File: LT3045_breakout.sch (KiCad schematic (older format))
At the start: 11 parts, among them J1 CONN_01X03, U1 LT3045EDD

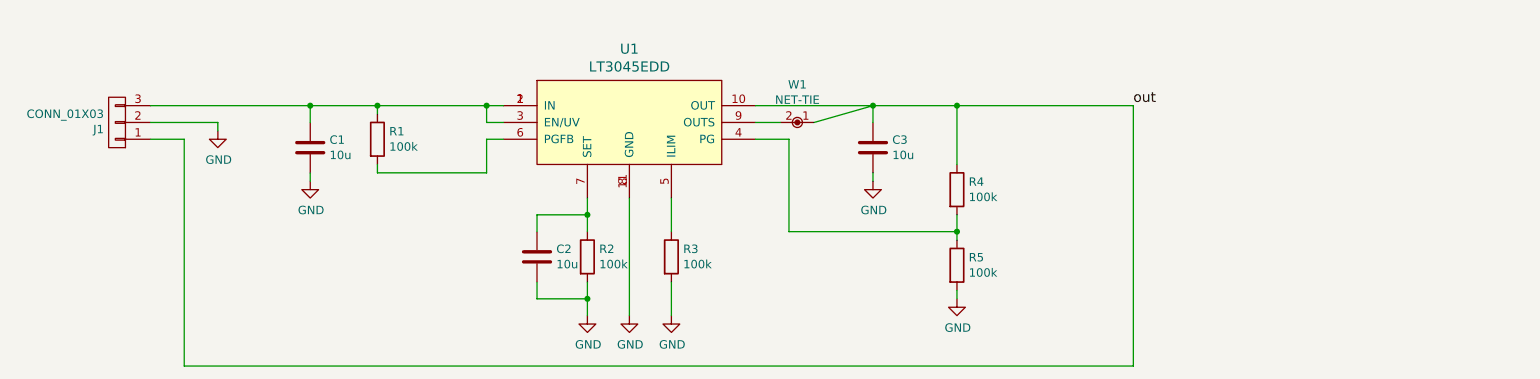
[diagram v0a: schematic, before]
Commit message: Removed PGFB pull resistor. We do not need that.
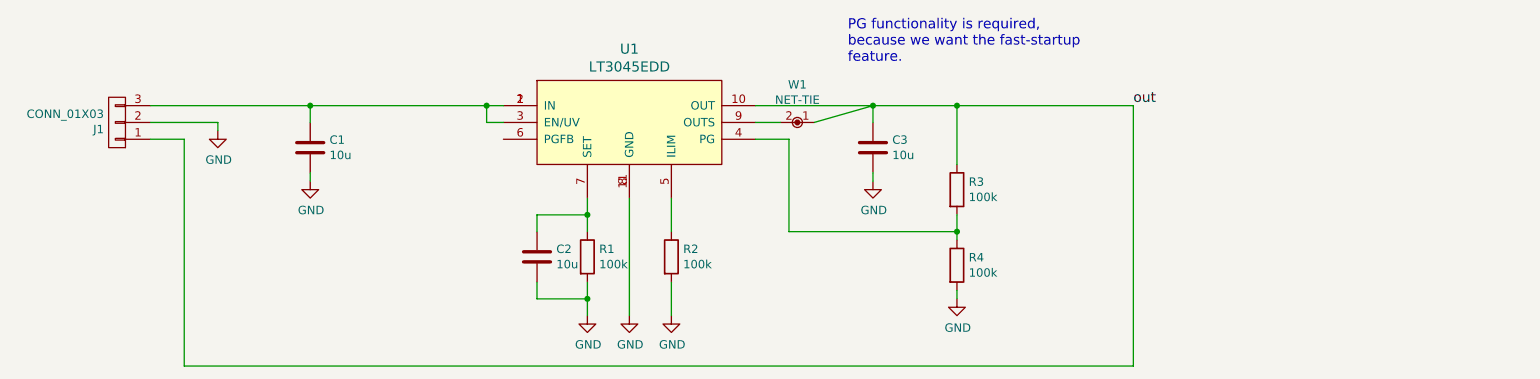
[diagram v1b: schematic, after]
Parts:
- removed R1: 100k, Resistors_SMD:R_0402, symbol R
- renumbered R2 to R1, R3 to R2, R4 to R3, R5 to R4
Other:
- note added: "PG functionality is required,\nbecause we want the fast-startup\nfeature."
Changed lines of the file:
@@
 LIBS:Linear Technology
 LIBS:net-tie
-LIBS:LT3045_breakout-cache
 EELAYER 26 0
 EELAYER END
@@
 $EndComp
 $Comp
-L GND #PWR01
+L GND #PWR1
 U 1 1 5989455D
 P 2600 2850
-F 0 "#PWR01" H 2600 2600 50  0001 C CNN
+F 0 "#PWR1" H 2600 2600 50  0001 C CNN
 F 1 "GND" H 2605 2677 50  0000 C CNN
 F 2 "" H 2600 2850 50  0001 C CNN
@@
 $EndComp
 Wire Wire Line
-	2200 2700 4300 2700
-$Comp
-L R R1
-U 1 1 59894789
-P 3550 2900
-F 0 "R1" H 3620 2946 50  0000 L CNN
-F 1 "100k" H 3620 2855 50  0000 L CNN
-F 2 "Resistors_SMD:R_0402" V 3480 2900 50  0001 C CNN
-F 3 "" H 3550 2900 50  0001 C CNN
-	1    3550 2900
-	1    0    0    -1
-$EndComp
-Wire Wire Line
-	3550 2700 3550 2750
-Connection ~ 3550 2700
-Wire Wire Line
-	3550 3050 3550 3100
-Wire Wire Line
-	3550 3100 4200 3100
-Wire Wire Line
-	4200 3100 4200 2900
-Wire Wire Line
-	4200 2900 4300 2900
-Wire Wire Line
 	4300 2800 4200 2800
 Wire Wire Line
@@
 Connection ~ 4200 2700
 $Comp
-L R R2
+L R R1
 U 1 1 5989486E
 P 4800 3600
-F 0 "R2" H 4870 3646 50  0000 L CNN
+F 0 "R1" H 4870 3646 50  0000 L CNN
 F 1 "100k" H 4870 3555 50  0000 L CNN
 F 2 "Resistors_SMD:R_0603" V 4730 3600 50  0001 C CNN
@@
 	4800 3750 4800 3950
 $Comp
-L GND #PWR02
+L GND #PWR3
 U 1 1 59894988
 P 4800 3950
-F 0 "#PWR02" H 4800 3700 50  0001 C CNN
+F 0 "#PWR3" H 4800 3700 50  0001 C CNN
 F 1 "GND" H 4805 3777 50  0000 C CNN
 F 2 "" H 4800 3950 50  0001 C CNN
@@
 	5050 3250 5050 3950
 $Comp
-L GND #PWR03
+L GND #PWR4
 U 1 1 598949D4
 P 5050 3950
-F 0 "#PWR03" H 5050 3700 50  0001 C CNN
+F 0 "#PWR4" H 5050 3700 50  0001 C CNN
 F 1 "GND" H 5055 3777 50  0000 C CNN
 F 2 "" H 5050 3950 50  0001 C CNN
@@
 $EndComp
 $Comp
-L R R3
+L R R2
 U 1 1 598949E9
 P 5300 3600
-F 0 "R3" H 5370 3646 50  0000 L CNN
+F 0 "R2" H 5370 3646 50  0000 L CNN
 F 1 "100k" H 5370 3555 50  0000 L CNN
 F 2 "Resistors_SMD:R_0603" V 5230 3600 50  0001 C CNN
@@
 $EndComp
 $Comp
-L GND #PWR04
+L GND #PWR5
 U 1 1 59894A27
 P 5300 3950
-F 0 "#PWR04" H 5300 3700 50  0001 C CNN
+F 0 "#PWR5" H 5300 3700 50  0001 C CNN
 F 1 "GND" H 5305 3777 50  0000 C CNN
 F 2 "" H 5300 3950 50  0001 C CNN
@@
 	6500 2700 6150 2800
 $Comp
-L R R4
-U 1 1 59894C9F
-P 7000 3200
-F 0 "R4" H 7070 3246 50  0000 L CNN
-F 1 "100k" H 7070 3155 50  0000 L CNN
-F 2 "Resistors_SMD:R_0402" V 6930 3200 50  0001 C CNN
-F 3 "" H 7000 3200 50  0001 C CNN
-	1    7000 3200
-	1    0    0    -1
-$EndComp
-$Comp
-L R R5
-U 1 1 59894D03
-P 7000 3650
-F 0 "R5" H 7070 3696 50  0000 L CNN
-F 1 "100k" H 7070 3605 50  0000 L CNN
-F 2 "Resistors_SMD:R_0402" V 6930 3650 50  0001 C CNN
-F 3 "" H 7000 3650 50  0001 C CNN
-	1    7000 3650
-	1    0    0    -1
-$EndComp
-Wire Wire Line
-	5800 2900 6000 2900
-Wire Wire Line
-	6000 2900 6000 3450
-Wire Wire Line
-	6000 3450 7000 3450
-Wire Wire Line
-	7000 3350 7000 3500
-Connection ~ 7000 3450
-$Comp
-L GND #PWR05
+L GND #PWR6
 U 1 1 59894DDD
 P 6500 3150
-F 0 "#PWR05" H 6500 2900 50  0001 C CNN
+F 0 "#PWR6" H 6500 2900 50  0001 C CNN
 F 1 "GND" H 6505 2977 50  0000 C CNN
 F 2 "" H 6500 3150 50  0001 C CNN
@@
 	1    0    0    -1
 $EndComp
-$Comp
-L GND #PWR06
-U 1 1 59894DFC
-P 7000 3850
-F 0 "#PWR06" H 7000 3600 50  0001 C CNN
-F 1 "GND" H 7005 3677 50  0000 C CNN
-F 2 "" H 7000 3850 50  0001 C CNN
-F 3 "" H 7000 3850 50  0001 C CNN
-	1    7000 3850
-	1    0    0    -1
-$EndComp
-Wire Wire Line
-	7000 3850 7000 3800
-Wire Wire Line
-	7000 2700 7000 3050
 Connection ~ 6500 2700
 Wire Wire Line
@@
 $EndComp
 $Comp
-L GND #PWR07
+L GND #PWR2
 U 1 1 59894F82
 P 3150 3150
-F 0 "#PWR07" H 3150 2900 50  0001 C CNN
+F 0 "#PWR2" H 3150 2900 50  0001 C CNN
 F 1 "GND" H 3155 2977 50  0000 C CNN
 F 2 "" H 3150 3150 50  0001 C CNN
@@
 Text Label 8050 2700 0    60   ~ 0
 out
+Wire Wire Line
+	7000 3850 7000 3800
+$Comp
+L GND #PWR7
+U 1 1 59894DFC
+P 7000 3850
+F 0 "#PWR7" H 7000 3600 50  0001 C CNN
+F 1 "GND" H 7005 3677 50  0000 C CNN
+F 2 "" H 7000 3850 50  0001 C CNN
+F 3 "" H 7000 3850 50  0001 C CNN
+	1    7000 3850
+	1    0    0    -1
+$EndComp
+Wire Wire Line
+	5800 2900 6000 2900
+Connection ~ 7000 3450
+Wire Wire Line
+	6000 2900 6000 3450
+Wire Wire Line
+	6000 3450 7000 3450
+Wire Wire Line
+	7000 3350 7000 3500
+$Comp
+L R R4
+U 1 1 59894D03
+P 7000 3650
+F 0 "R4" H 7070 3696 50  0000 L CNN
+F 1 "100k" H 7070 3605 50  0000 L CNN
+F 2 "Resistors_SMD:R_0402" V 6930 3650 50  0001 C CNN
+F 3 "" H 7000 3650 50  0001 C CNN
+	1    7000 3650
+	1    0    0    -1
+$EndComp
+Wire Wire Line
+	7000 2700 7000 3050
+$Comp
+L R R3
+U 1 1 59894C9F
+P 7000 3200
+F 0 "R3" H 7070 3246 50  0000 L CNN
+F 1 "100k" H 7070 3155 50  0000 L CNN
+F 2 "Resistors_SMD:R_0402" V 6930 3200 50  0001 C CNN
+F 3 "" H 7000 3200 50  0001 C CNN
+	1    7000 3200
+	1    0    0    -1
+$EndComp
+Text Notes 6350 2450 0    60   ~ 0
+PG functionality is required,\nbecause we want the fast-startup\nfeature.
+Wire Wire Line
+	2200 2700 4300 2700
 $EndSCHEMATC

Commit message: Changed resistor values to outout 12V@500mA
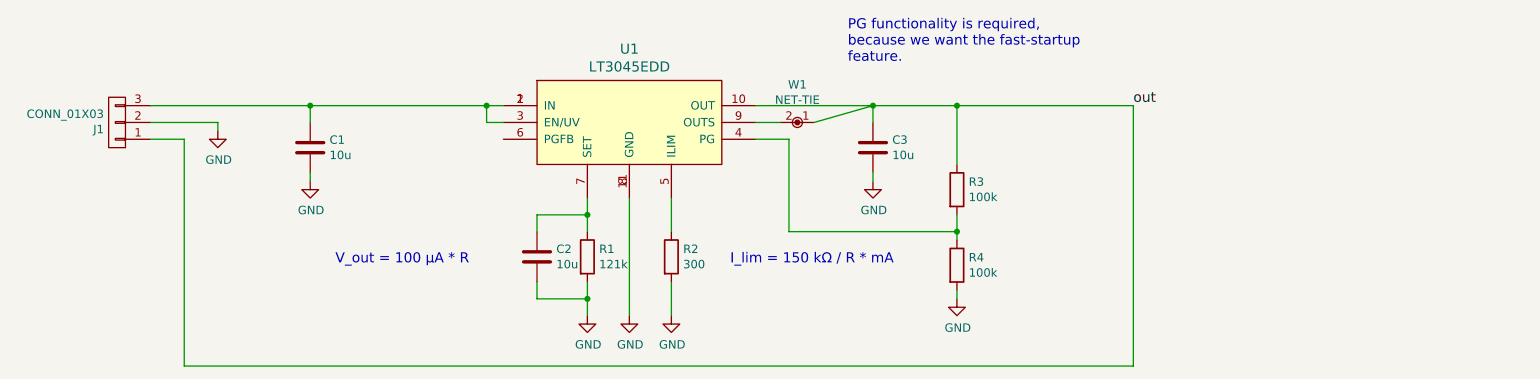
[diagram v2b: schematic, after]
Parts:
- R1: value 100k -> 121k
- R2: value 100k -> 300
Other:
- note added: "I_lim = 150 kΩ / R * mA"
- note added: "V_out = 100 µA * R"
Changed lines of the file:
@@
 LIBS:Linear Technology
 LIBS:net-tie
+LIBS:LT3045_breakout-cache
 EELAYER 26 0
 EELAYER END
@@
 P 4800 3600
 F 0 "R1" H 4870 3646 50  0000 L CNN
-F 1 "100k" H 4870 3555 50  0000 L CNN
+F 1 "121k" H 4870 3555 50  0000 L CNN
 F 2 "Resistors_SMD:R_0603" V 4730 3600 50  0001 C CNN
 F 3 "" H 4800 3600 50  0001 C CNN
@@
 P 5300 3600
 F 0 "R2" H 5370 3646 50  0000 L CNN
-F 1 "100k" H 5370 3555 50  0000 L CNN
+F 1 "300" H 5370 3555 50  0000 L CNN
 F 2 "Resistors_SMD:R_0603" V 5230 3600 50  0001 C CNN
 F 3 "" H 5300 3600 50  0001 C CNN
@@
 Wire Wire Line
 	2200 2700 4300 2700
+Text Notes 3300 3650 0    60   ~ 0
+V_out = 100 µA * R
+Text Notes 5650 3650 0    60   ~ 0
+I_lim = 150 kΩ / R * mA
 $EndSCHEMATC

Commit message: Updated to v1.1 Added BOM Removed old gerber files Updated component values on the pcb board
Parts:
- J1: symbol CONN_01X03 -> Conn_01x03_Male; MFN (none) -> Amphenol; MFP (none) -> 68016-403HLF
- R1: value 121k -> 120k; MFN (none) -> Susumu; MFP (none) -> RR0816P-124-D
- R2: MFN (none) -> Susumu; MFP (none) -> RR0816P-301-D
- R3: value 100k -> 200k; MFN (none) -> Vishay; MFP (none) -> MCS04020C2003FE000
- R4: value 100k -> 5.6k; MFN (none) -> Susumu; MFP (none) -> RR0510P-562-D
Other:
- note added: "V_PG = 0.3 V * (1 + R3/R2)"
- note added: "Values R1, R2, R3 were calculated for\nVout = 12 V\nV_PG = 11 V"
- moved on the sheet: C2
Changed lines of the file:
@@
 encoding utf-8
 Sheet 1 1
-Title ""
-Date ""
-Rev ""
+Title "LT3045 Breakout Board"
+Date "2017-12-14"
+Rev "v1.1"
 Comp ""
-Comment1 ""
-Comment2 ""
+Comment1 "Copyright (©) 2017, Patrick Baus <patrick.baus@physik.tu-darmstadt.de>"
+Comment2 "Licensed under CERN OHL v.1.2"
 Comment3 ""
 Comment4 ""
 $EndDescr
 $Comp
-L CONN_01X03 J1
+L Conn_01x03_Male J1
 U 1 1 598944A2
 P 2000 2800
-F 0 "J1" H 2078 2841 50  0000 L CNN
-F 1 "CONN_01X03" H 2078 2750 50  0000 L CNN
+F 0 "J1" H 1850 2850 50  0000 L CNN
+F 1 "CONN_01X03" H 1450 2700 50  0000 L CNN
 F 2 "Pin_Headers:Pin_Header_Angled_1x03_Pitch2.54mm" H 2000 2800 50  0001 C CNN
 F 3 "" H 2000 2800 50  0001 C CNN
+F 4 "Amphenol" H 2000 2800 60  0001 C CNN "MFN"
+F 5 "68016-403HLF" H 2000 2800 60  0001 C CNN "MFP"
 	1    2000 2800
-	-1   0    0    1
-$EndComp
-$Comp
-L GND #PWR1
+	1    0    0    1
+$EndComp
+$Comp
+L GND #PWR01
 U 1 1 5989455D
 P 2600 2850
-F 0 "#PWR1" H 2600 2600 50  0001 C CNN
+F 0 "#PWR01" H 2600 2600 50  0001 C CNN
 F 1 "GND" H 2605 2677 50  0000 C CNN
 F 2 "" H 2600 2850 50  0001 C CNN
@@
 P 4800 3600
 F 0 "R1" H 4870 3646 50  0000 L CNN
-F 1 "121k" H 4870 3555 50  0000 L CNN
+F 1 "120k" H 4870 3555 50  0000 L CNN
 F 2 "Resistors_SMD:R_0603" V 4730 3600 50  0001 C CNN
 F 3 "" H 4800 3600 50  0001 C CNN
+F 4 "Susumu" H 4800 3600 60  0001 C CNN "MFN"
+F 5 "RR0816P-124-D" H 4800 3600 60  0001 C CNN "MFP"
 	1    4800 3600
 	1    0    0    -1
@@
 	4800 3250 4800 3450
 Wire Wire Line
-	4800 3350 4500 3350
-Wire Wire Line
-	4500 3350 4500 3450
+	4800 3350 4450 3350
+Wire Wire Line
+	4450 3350 4450 3450
 Connection ~ 4800 3350
 Wire Wire Line
-	4500 3750 4500 3850
-Wire Wire Line
-	4500 3850 4800 3850
+	4450 3750 4450 3850
+Wire Wire Line
+	4450 3850 4800 3850
 Wire Wire Line
 	4800 3750 4800 3950
 $Comp
-L GND #PWR3
+L GND #PWR02
 U 1 1 59894988
 P 4800 3950
-F 0 "#PWR3" H 4800 3700 50  0001 C CNN
+F 0 "#PWR02" H 4800 3700 50  0001 C CNN
 F 1 "GND" H 4805 3777 50  0000 C CNN
 F 2 "" H 4800 3950 50  0001 C CNN
@@
 	5050 3250 5050 3950
 $Comp
-L GND #PWR4
+L GND #PWR03
 U 1 1 598949D4
 P 5050 3950
-F 0 "#PWR4" H 5050 3700 50  0001 C CNN
+F 0 "#PWR03" H 5050 3700 50  0001 C CNN
 F 1 "GND" H 5055 3777 50  0000 C CNN
 F 2 "" H 5050 3950 50  0001 C CNN
@@
 F 2 "Resistors_SMD:R_0603" V 5230 3600 50  0001 C CNN
 F 3 "" H 5300 3600 50  0001 C CNN
+F 4 "Susumu" H 5300 3600 60  0001 C CNN "MFN"
+F 5 "RR0816P-301-D" H 5300 3600 60  0001 C CNN "MFP"
 	1    5300 3600
 	1    0    0    -1
 $EndComp
 $Comp
-L GND #PWR5
+L GND #PWR04
 U 1 1 59894A27
 P 5300 3950
-F 0 "#PWR5" H 5300 3700 50  0001 C CNN
+F 0 "#PWR04" H 5300 3700 50  0001 C CNN
 F 1 "GND" H 5305 3777 50  0000 C CNN
 F 2 "" H 5300 3950 50  0001 C CNN
@@
 	6500 2700 6150 2800
 $Comp
-L GND #PWR6
+L GND #PWR05
 U 1 1 59894DDD
 P 6500 3150
-F 0 "#PWR6" H 6500 2900 50  0001 C CNN
+F 0 "#PWR05" H 6500 2900 50  0001 C CNN
 F 1 "GND" H 6505 2977 50  0000 C CNN
 F 2 "" H 6500 3150 50  0001 C CNN
@@
 $EndComp
 $Comp
-L GND #PWR2
+L GND #PWR06
 U 1 1 59894F82
 P 3150 3150
-F 0 "#PWR2" H 3150 2900 50  0001 C CNN
+F 0 "#PWR06" H 3150 2900 50  0001 C CNN
 F 1 "GND" H 3155 2977 50  0000 C CNN
 F 2 "" H 3150 3150 50  0001 C CNN
@@
 L C C2
 U 1 1 59895DC4
-P 4500 3600
-F 0 "C2" H 4615 3646 50  0000 L CNN
-F 1 "10u" H 4615 3555 50  0000 L CNN
-F 2 "Capacitors_SMD:C_0603" H 4538 3450 50  0001 C CNN
-F 3 "" H 4500 3600 50  0001 C CNN
-F 4 "Murata" H 4500 3600 60  0001 C CNN "MFN"
-F 5 "GRM188R6YA106MA73D" H 4500 3600 60  0001 C CNN "MFP"
-F 6 "GRM188R6YA475KE15D" H 4500 3600 60  0001 C CNN "Alternative"
-	1    4500 3600
+P 4450 3600
+F 0 "C2" H 4565 3646 50  0000 L CNN
+F 1 "10u" H 4565 3555 50  0000 L CNN
+F 2 "Capacitors_SMD:C_0603" H 4488 3450 50  0001 C CNN
+F 3 "" H 4450 3600 50  0001 C CNN
+F 4 "Murata" H 4450 3600 60  0001 C CNN "MFN"
+F 5 "GRM188R6YA106MA73D" H 4450 3600 60  0001 C CNN "MFP"
+F 6 "GRM188R6YA475KE15D" H 4450 3600 60  0001 C CNN "Alternative"
+	1    4450 3600
 	1    0    0    -1
 $EndComp
@@
 	7000 3850 7000 3800
 $Comp
-L GND #PWR7
+L GND #PWR07
 U 1 1 59894DFC
 P 7000 3850
-F 0 "#PWR7" H 7000 3600 50  0001 C CNN
+F 0 "#PWR07" H 7000 3600 50  0001 C CNN
 F 1 "GND" H 7005 3677 50  0000 C CNN
 F 2 "" H 7000 3850 50  0001 C CNN
@@
 P 7000 3650
 F 0 "R4" H 7070 3696 50  0000 L CNN
-F 1 "100k" H 7070 3605 50  0000 L CNN
+F 1 "5.6k" H 7070 3605 50  0000 L CNN
 F 2 "Resistors_SMD:R_0402" V 6930 3650 50  0001 C CNN
 F 3 "" H 7000 3650 50  0001 C CNN
+F 4 "Susumu" H 7000 3650 60  0001 C CNN "MFN"
+F 5 "RR0510P-562-D" H 7000 3650 60  0001 C CNN "MFP"
 	1    7000 3650
 	1    0    0    -1
@@
 P 7000 3200
 F 0 "R3" H 7070 3246 50  0000 L CNN
-F 1 "100k" H 7070 3155 50  0000 L CNN
+F 1 "200k" H 7070 3155 50  0000 L CNN
 F 2 "Resistors_SMD:R_0402" V 6930 3200 50  0001 C CNN
 F 3 "" H 7000 3200 50  0001 C CNN
+F 4 "Vishay" H 7000 3200 60  0001 C CNN "MFN"
+F 5 "MCS04020C2003FE000" H 7000 3200 60  0001 C CNN "MFP"
 	1    7000 3200
 	1    0    0    -1
@@
 Text Notes 5650 3650 0    60   ~ 0
 I_lim = 150 kΩ / R * mA
+Text Notes 7300 3450 0    60   ~ 0
+V_PG = 0.3 V * (1 + R3/R2)
+Text Notes 8250 3100 0    60   ~ 0
+Values R1, R2, R3 were calculated for\nVout = 12 V\nV_PG = 11 V
 $EndSCHEMATC

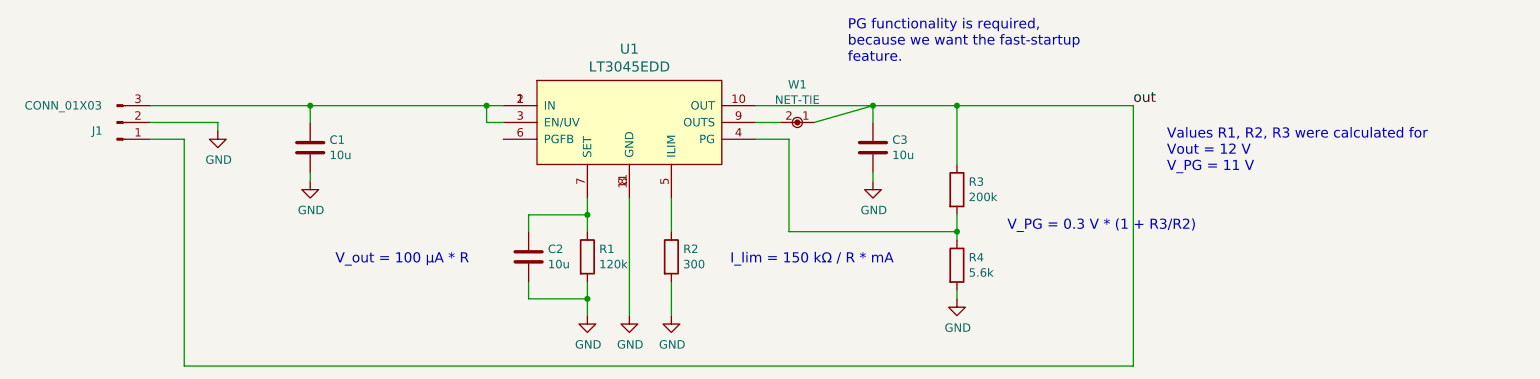
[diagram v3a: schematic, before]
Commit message: Updated libraries
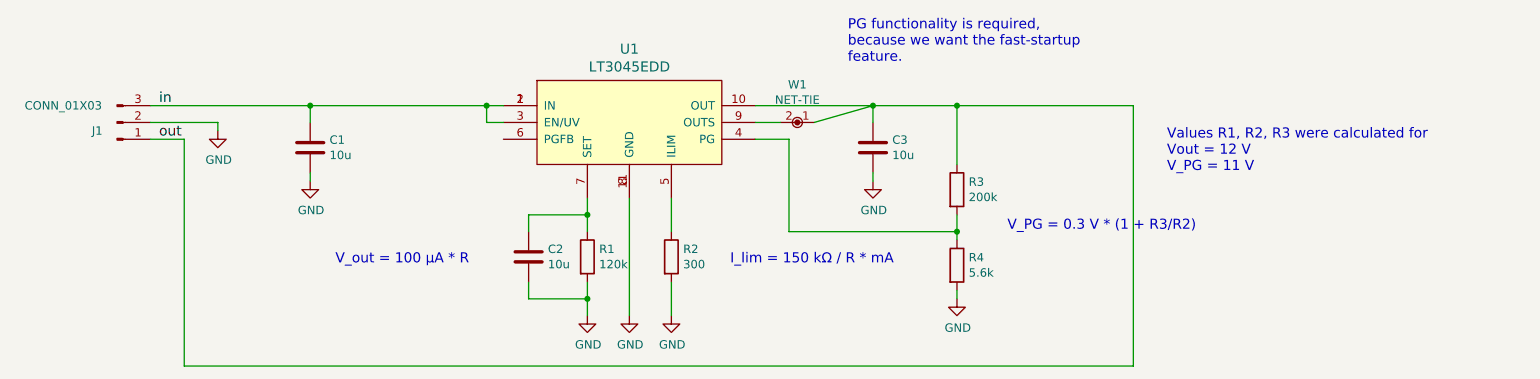
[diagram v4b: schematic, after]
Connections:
- net in: now reaches C1.1, J1.3 (Pin_3), U1.1 (IN), U1.2 (IN), U1.3 (EN/UV)
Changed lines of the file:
@@
 	8050 4250 8050 2700
 Connection ~ 7000 2700
-Text Label 8050 2700 0    60   ~ 0
+Text Label 2250 2900 0    60   ~ 0
 out
 Wire Wire Line
@@
 Text Notes 8250 3100 0    60   ~ 0
 Values R1, R2, R3 were calculated for\nVout = 12 V\nV_PG = 11 V
+Text Label 2250 2700 0    60   ~ 0
+in
 $EndSCHEMATC
